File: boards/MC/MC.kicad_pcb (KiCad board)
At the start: 2 copper layers, 120 x 102 mm, 27 parts, among them U1 CJMCU-9548, U2 КР293КП2Б, X1 B4B-XH-A, X10 B4B-XH-A, X2 B2P-VH, X3 B2B-XH-A, X4 B2B-XH-A, X5 B2P-VH, X6 BH-12, X7 BH-12, X8 BH-12, X9 BH-12

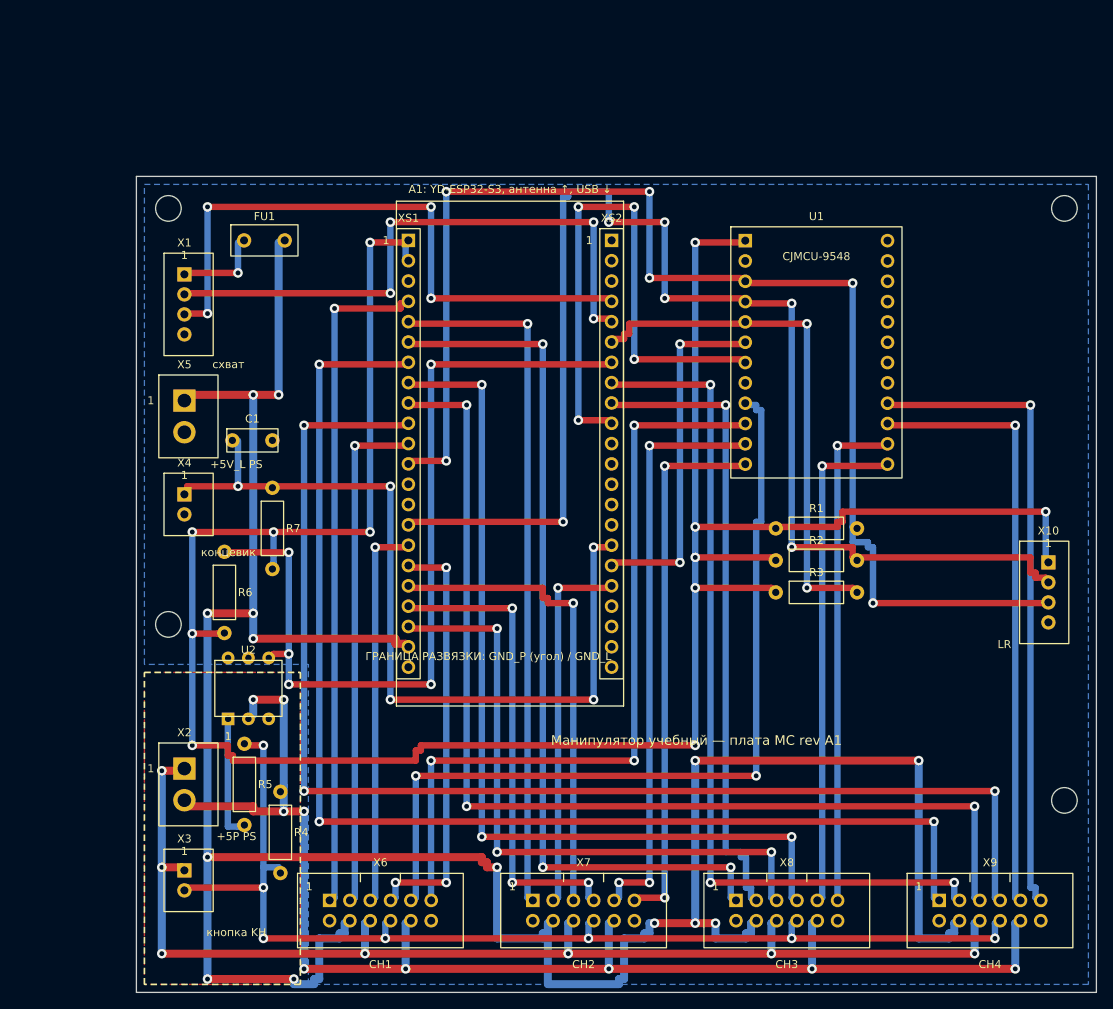
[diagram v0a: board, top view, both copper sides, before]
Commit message: Платы PS, MC, CH, LR: расстановка, трассировка, 3D-модели посадочных мест
PS:
- разведена по расстановке из файла: +24V_IN 6 мм (участок у K1 — 4 мм),
  шина +24V 6 мм с отводами 3 мм, +5P 2 мм, остров U2 1,5 мм;
  заливка GND_P на B.Cu, вырез заливки под островом, вырезы ⌀8 у крепежа
- классы цепей в PS.kicad_pro: Default, Power5, Power24, Island
- U1: посадочное место под модуль XL4015E 54 × 24 × 15 на штырях
  (пятаки IN/OUT, 2 стойки М3) по чертежу продавца; переразведены
  OUT+ и отвод +24V к IN+

MC:
- X5 перенесён, переразведены KH, +5P, GND_P в этой зоне
- FU1: место под Bourns MF-R110 (корпус 8,9 × 3,0 × 14,0)

CH:
- K1…K5, X5: места исправлены по datasheet (NRP-02, HF49FD, JST VH),
  переразведены цепи реле

LR:
- плата перекомпонована: X5…X8 — B5B-XH-A, как X1…X4; группы M1…M4
  по одному образцу (индикатор, разъём, защита в два ряда);
  X1…X4, X9 и DD1 на нижней стороне
- контур 176 × 59, 6 отверстий М3; разведена: сигналы F.Cu,
  GND_L заливкой B.Cu
- scripts/gen_LR_pcb.py удалён: описывал прежнюю раскладку с клеммами

Схемы:
- CH: X5 — JST VH (таблица Tbl_X5_CH_VH); MC: X3 — B4B-XH-A
  (кнопка KH с индикатором); PS: X11 убран; LR: у X5…X8 место
  B5B-XH-A
- sch_common: генератор не перезаписывает файл, сохранённый KiCad,
  без --force

3D-модели (lib/3dmodels):
- упрощённые по чертежам datasheet: NRP-02, HF49FD, NRP-15 (корпус),
  JST B2P-VH, Mornsun/K-CUT URB2405YMD (U2), Talema DPO-3.0-22 (кольцо
  лежит), Bourns MF-R110
- из библиотеки KiCad: PinSocket 1×3, 1×4, 1×12, Phoenix MKDS-1,5-2
- docs/3D-модели.md — источники размеров и что сверить

База компонентов: E-083 — Bourns MF-R110 (Ihold 1,1 А), «Выбран»;
csv перевыгружены
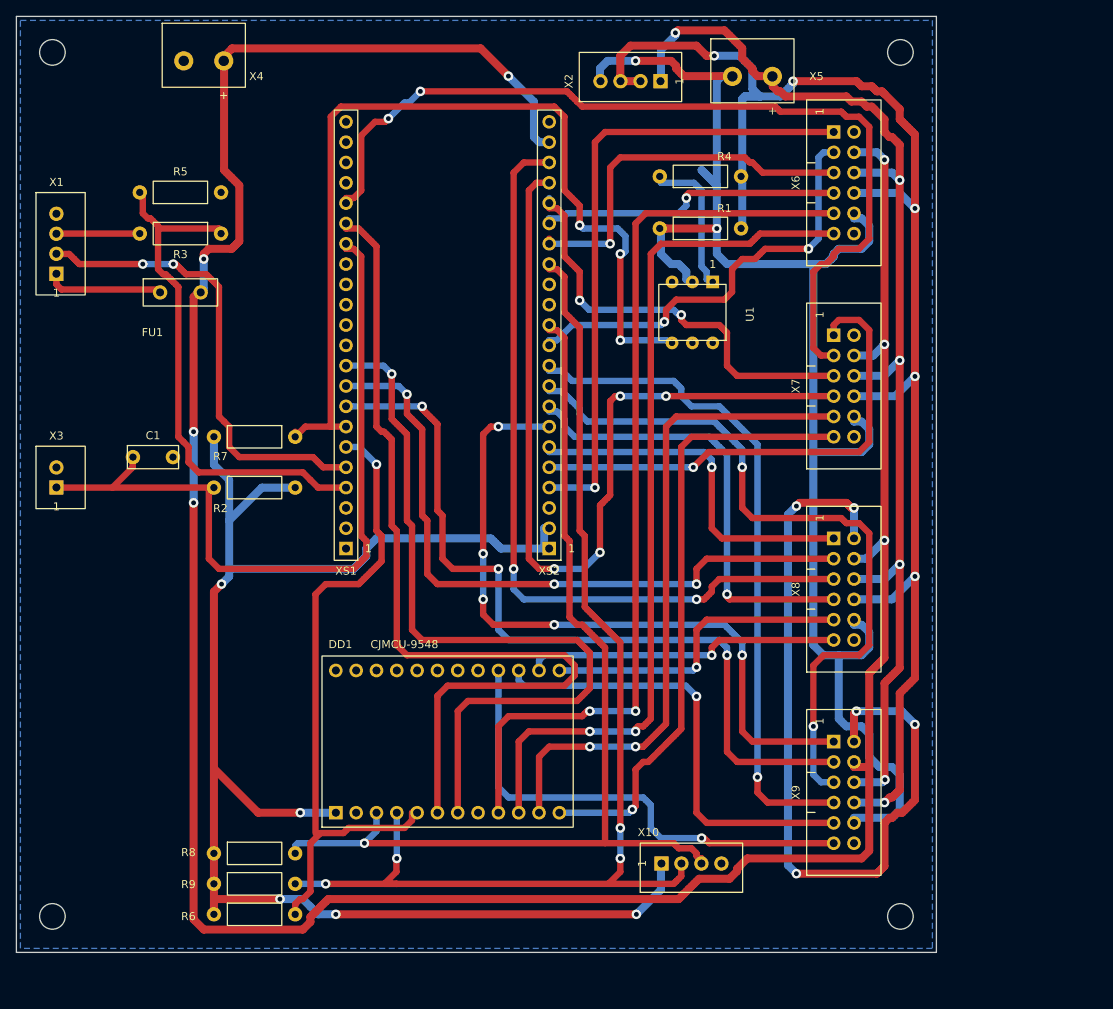
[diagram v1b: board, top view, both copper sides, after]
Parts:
- removed U2: КР293КП2Б, manipulator:DIP-6_W7.62mm_H
- added DD1: CJMCU-9548, manipulator:Module_CJMCU-9548, F.Cu at (88.9, 120.7)
- added R8: 4,7 кОм, manipulator:R_Axial_P10.16mm, F.Cu at (64.8, 134.6)
- added R9: 4,7 кОм, manipulator:R_Axial_P10.16mm, F.Cu at (64.8, 138.4)
- R1: value 4,7 кОм -> 1 кОм; footprint manipulator:R_Axial_P10.16mm -> manipulator:R_Axial_P10.16mm_V
- R2: value 4,7 кОм -> 10 кОм; footprint manipulator:R_Axial_P10.16mm -> manipulator:R_Axial_P10.16mm_V
- R3: footprint manipulator:R_Axial_P10.16mm -> manipulator:R_Axial_P10.16mm_V
- R4: value 1 кОм -> 470 Ом
- R5: value 470 Ом -> 20 кОм
- R6: footprint manipulator:R_Axial_P10.16mm_V -> manipulator:R_Axial_P10.16mm
- U1: value CJMCU-9548 -> КР293КП2Б; footprint manipulator:Module_CJMCU-9548 -> manipulator:DIP-6_W7.62mm_H
- X2: value B2P-VH -> B4B-XH-A; footprint manipulator:JST_VH_B2P-VH_L -> manipulator:JST_XH_B4B-XH-A_L
- X4: value B2B-XH-A -> DG301-5.0-02P; footprint manipulator:JST_XH_B2B-XH-A_L -> manipulator:TB_DG301-5.0_2P_R
- X5: value B2P-VH -> DG301-5.0-02P; footprint manipulator:JST_VH_B2P-VH_L -> manipulator:TB_DG301-5.0_2P_R
- X6, X7, X8, X9: value BH-12 -> BH-12 (2×6)
- moved X6 107.8 mm to (138.4, 50.8), turned to 90 degrees
- moved X2 104.1 mm to (111.8, 38.1), turned to 90 degrees
- moved R4 97.4 mm to (120.5, 50.0), turned to 90 degrees
- moved R3 91.3 mm to (55.5, 57.1), turned to -90 degrees
- moved X5 82.7 mm to (127.0, 37.5)
- moved R5 74.4 mm to (55.5, 52.0), turned to 90 degrees
- moved X7 73.2 mm to (138.4, 76.2), turned to 90 degrees
- moved R2 70.8 mm to (64.8, 88.9), turned to 90 degrees
- moved X10 56.0 mm to (119.4, 135.9), turned to 90 degrees
- moved X4 55.5 mm to (58.4, 35.6)
- moved X3 52.9 mm to (40.0, 87.6)
- moved X8 40.8 mm to (138.4, 101.6), turned to 90 degrees
- moved R6 40.4 mm to (64.8, 142.2)
- moved R1 40.2 mm to (120.5, 56.5), turned to 90 degrees
- moved XS1 39.3 mm to (76.2, 96.5), turned to 180 degrees
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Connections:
- C1 pad 1: Net-(XS2-IO48) -> Net-(X3-SW1)
- R1 pad 1: 3V3 -> KH
- R1 pad 2: SDA -> GND_P
- R2 pad 2: SCL -> Net-(X3-SW1)
- R3 pad 1: 3V3 -> Net-(X1-RX)
- R3 pad 2: MUX-RST -> Net-(XS1-IO1)
- R4 pad 2: GND_P -> Net-(U1-A)
- R5 pad 1: Net-(R5-Pad1) -> GND_L
- R5 pad 2: KH -> Net-(XS1-IO1)
- R6 pad 2: Net-(U2-OUT) -> MUX-RST
- R7 pad 2: Net-(XS2-IO48) -> Net-(XS1-IO41)
- U1 pad 1: 3V3 -> Net-(U1-A)
- U1 pad 2: SDA -> GND_P
- U1 pad 3: SCL -> (no net)
- U1 pad 4: MUX-RST -> Net-(XS1-IO41)
- U1 pad 5: MUX-A0 -> (no net)
- U1 pad 6: MUX-A1 -> GND_L
- X1 pad 2: Net-(XS2-IO2) -> Net-(X1-TX)
- X1 pad 3: Net-(XS2-IO1) -> Net-(X1-RX)
- X10 pad 2: SCL -> Net-(DD1-SCL)
- X10 pad 3: SDA -> Net-(DD1-SDA)
- X2 pad 2: GND_P -> KH
- X3 pad 1: +5P -> Net-(X3-SW1)
- X3 pad 2: KH -> GND_L
- X4 pad 1: Net-(XS2-IO48) -> +5V_L
- X5 pad 1: +5V_L -> +5P
- X5 pad 2: GND_L -> GND_P
- X6 pad 1: M1_CURR -> Net-(X6-M1_CURR)
- X6 pad 3: M1_RELE -> Net-(X6-M1_RELE)
- X6 pad 5: M1_IN1 -> Net-(X6-M1_IN1)
- X6 pad 7: M1_IN2 -> Net-(X6-M1_IN2)
- X7 pad 1: M2_CURR -> Net-(X7-M2_CURR)
- X7 pad 5: M2_IN1 -> Net-(X7-M2_IN1)
- X7 pad 7: M2_IN2 -> Net-(X7-M2_IN2)
- X8 pad 1: M3_CURR -> Net-(X8-M3_CURR)
- X8 pad 5: M3_IN1 -> Net-(X8-M3_IN1)
- X8 pad 7: M3_IN2 -> Net-(X8-M3_IN2)
- X9 pad 1: M4_CURR -> Net-(X9-M4_CURR)
- X9 pad 5: M4_IN1 -> Net-(X9-M4_IN1)
- X9 pad 7: M4_IN2 -> Net-(X9-M4_IN2)
- XS1 pad 1: 3V3 -> GND_L
- XS1 pad 10: M4_IN2 -> MUX-A1
- XS1 pad 11: M1_RELE -> unconnected-(XS1-IO37-Pad11)
- XS1 pad 12: SDA -> unconnected-(XS1-IO36-Pad12)
- XS1 pad 15: SCL -> unconnected-(XS1-IO45-Pad15)
- XS1 pad 16: M1_IN1 -> Net-(X3-SW1)
- XS1 pad 17: M1_IN2 -> MUX-A0
- XS1 pad 18: M2_IN1 -> M2_RELE
- XS1 pad 19: M2_IN2 -> unconnected-(XS1-IO20-Pad19)
- XS1 pad 2: 3V3 -> unconnected-(XS1-TX-Pad2)
- XS1 pad 20: M3_IN1 -> unconnected-(XS1-IO19-Pad20)
- XS1 pad 21: +5V_L -> GND_L
- XS1 pad 4: M1_CURR -> Net-(XS1-IO1)
- XS1 pad 5: M2_CURR -> Net-(X1-TX)
- XS1 pad 6: M3_CURR -> MUX-RST
- XS1 pad 7: M4_CURR -> Net-(XS1-IO41)
- XS1 pad 8: M3_IN2 -> M4_RELE
- XS1 pad 9: M4_IN1 -> M3_RELE
- XS2 pad 1: GND_L -> 3V3
- XS2 pad 10: MUX-A1 -> Net-(X9-M4_IN2)
- XS2 pad 11: unconnected-(XS2-IO37-Pad11) -> Net-(X6-M1_RELE)
- XS2 pad 12: unconnected-(XS2-IO36-Pad12) -> Net-(DD1-SDA)
- XS2 pad 15: unconnected-(XS2-IO45-Pad15) -> Net-(DD1-SCL)
- XS2 pad 16: Net-(XS2-IO48) -> Net-(X6-M1_IN1)
- XS2 pad 17: MUX-A0 -> Net-(X6-M1_IN2)
- XS2 pad 18: M2_RELE -> Net-(X7-M2_IN1)
- XS2 pad 19: unconnected-(XS2-IO20-Pad19) -> Net-(X7-M2_IN2)
- XS2 pad 2: unconnected-(XS2-TX-Pad2) -> 3V3
- XS2 pad 20: unconnected-(XS2-IO19-Pad20) -> Net-(X8-M3_IN1)
- XS2 pad 21: GND_L -> +5V_L
- XS2 pad 4: Net-(XS2-IO1) -> Net-(X6-M1_CURR)
- XS2 pad 5: Net-(XS2-IO2) -> Net-(X7-M2_CURR)
- XS2 pad 6: MUX-RST -> Net-(X8-M3_CURR)
- XS2 pad 7: Net-(U2-OUT) -> Net-(X9-M4_CURR)
- XS2 pad 8: M4_RELE -> Net-(X8-M3_IN2)
- XS2 pad 9: M3_RELE -> Net-(X9-M4_IN1)
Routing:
- net SCL: track 168.8 -> 0.00 mm, vias 6 -> 0
- net SDA: track 164.0 -> 0.00 mm, vias 6 -> 0
- net M4_IN2: track 158.8 -> 0.00 mm, vias 3 -> 0
- net M4_CURR: track 155.0 -> 0.00 mm, vias 3 -> 0
- net Net-(DD1-SCL): track 0.00 -> 143.7 mm, vias 0 -> 4
- net M4_IN1: track 132.8 -> 0.00 mm, vias 3 -> 0
- net Net-(DD1-SDA): track 0.00 -> 126.5 mm, vias 0 -> 1
- net Net-(XS1-IO41): track 0.00 -> 117.1 mm, vias 0 -> 3
- net M3_IN2: track 112.5 -> 0.00 mm, vias 3 -> 0
- net 3V3: track 309.7 -> 197.7 mm, vias 12 -> 5
- net M3_CURR: track 110.0 -> 0.00 mm, vias 3 -> 0
- net Net-(U2-OUT): track 107.3 -> 0.00 mm, vias 5 -> 0
- net Net-(X7-M2_IN2): track 0.00 -> 106.9 mm, vias 0 -> 4
- net Net-(XS2-IO48): track 106.2 -> 0.00 mm, vias 5 -> 0
- net GND_L: track 0.00 -> 101.5 mm, vias 0 -> 5
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- removed copper zone on F.Cu, net GND_P
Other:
- board size 120 x 102 mm -> 115 x 117 mm
- rule pad_to_mask_clearance: 0.05 -> 0
- board text removed: "+5P PS"
- board text removed: "+5V_L PS"
- board text removed: "A1: YD-ESP32-S3, антенна ↑, USB ↓"
- board text removed: "CH1"
- board text removed: "CH2"
- board text removed: "CH3"
- board text removed: "CH4"
- board text removed: "LR"
- board text removed: "ГРАНИЦА РАЗВЯЗКИ: GND_P (угол) / GND_L"
- board text removed: "Манипулятор учебный — плата MC rev A1"
- board text removed: "кнопка KH"
- board text removed: "концевик"
- board text removed: "схват"
